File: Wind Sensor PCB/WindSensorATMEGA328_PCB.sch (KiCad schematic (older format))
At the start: 5 parts, among them P1 I2C, P2 SERIAL, P5 LOGO2, P6 PCB, P7 ENC

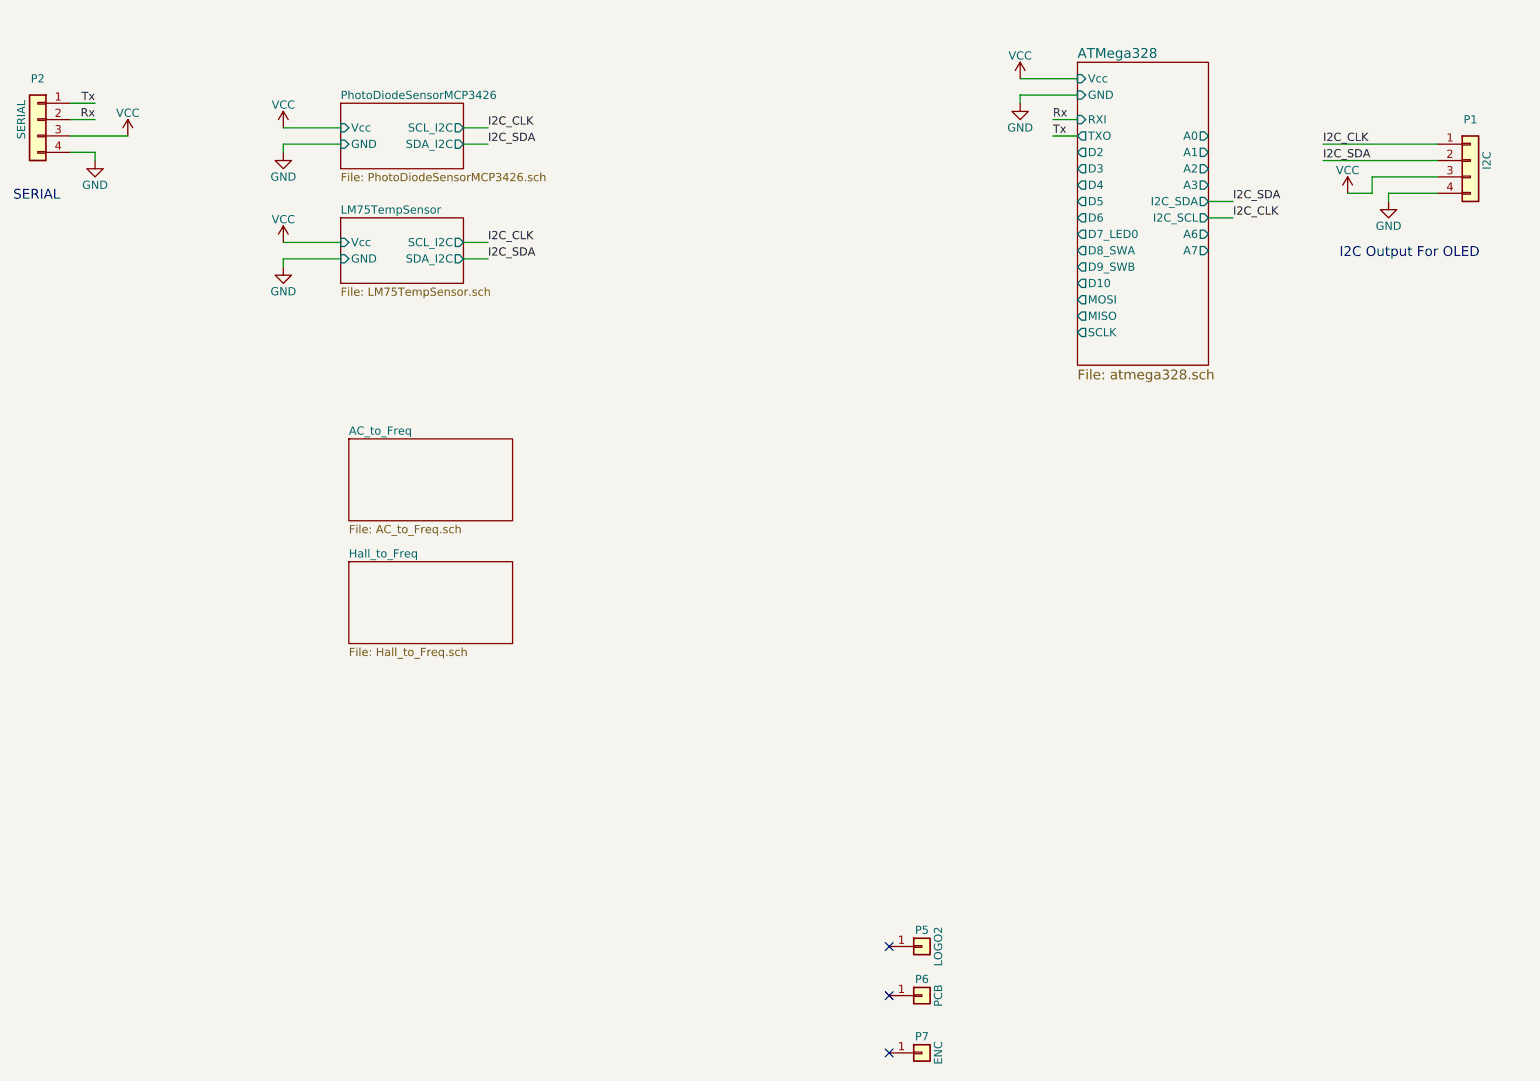
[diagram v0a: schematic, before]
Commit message: Updated PCB
Version 1 of the PCB with ATMEGA328 used...
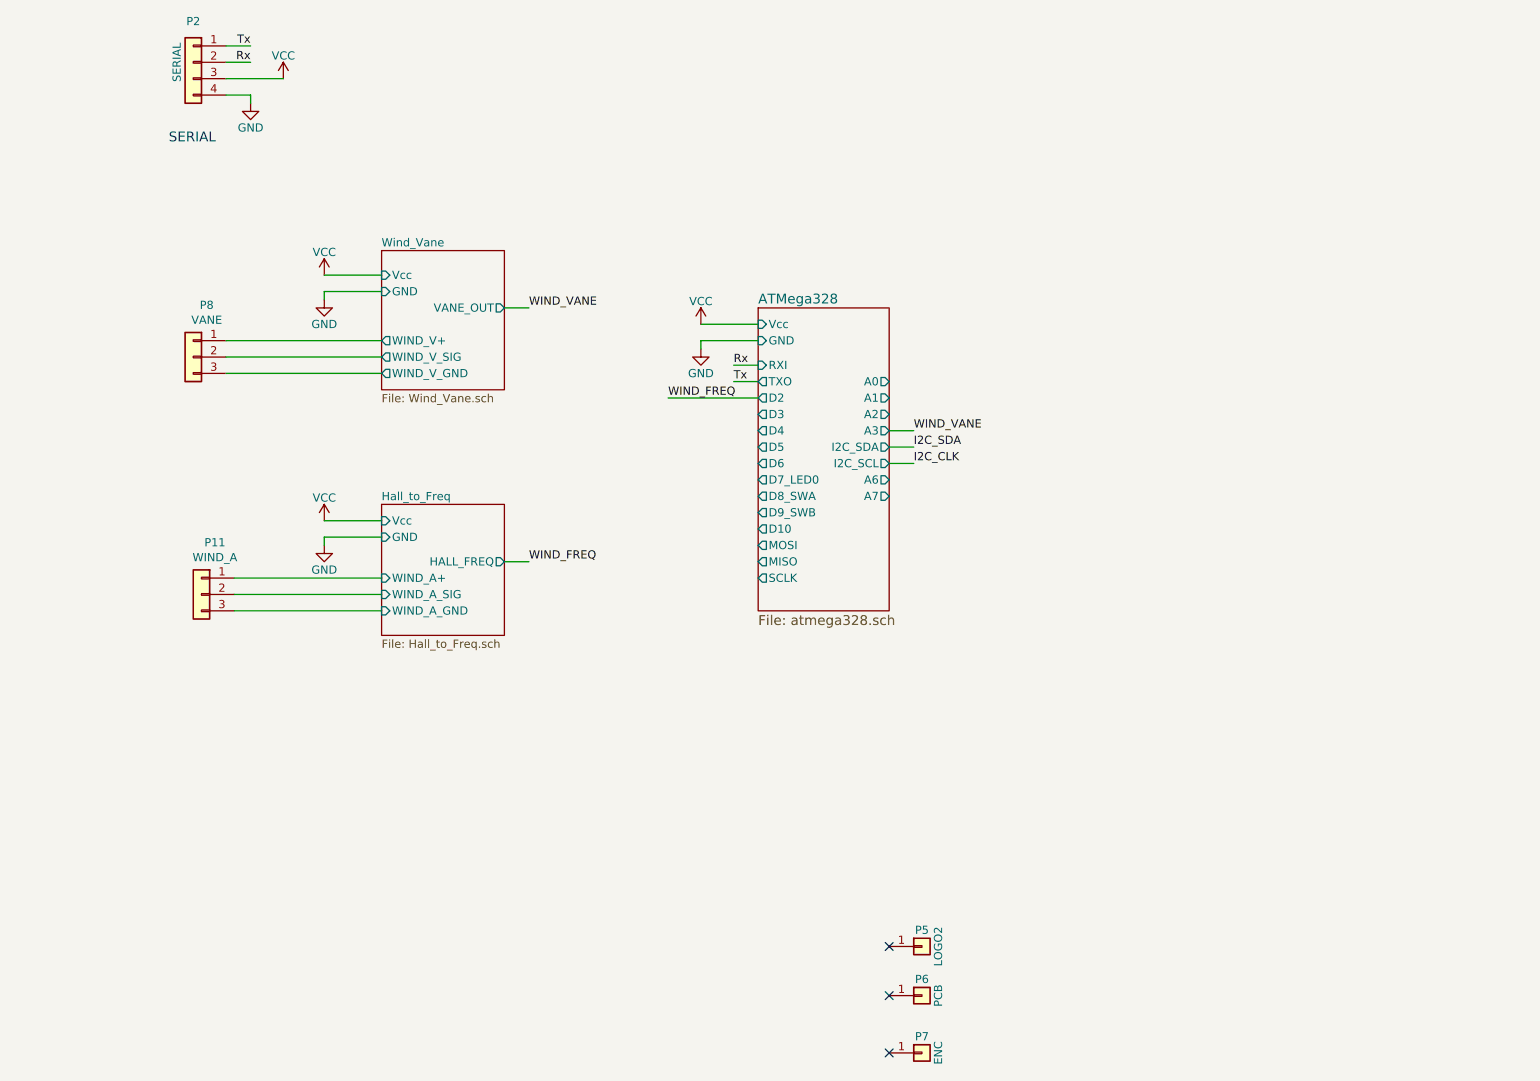
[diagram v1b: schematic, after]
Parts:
- removed P1: I2C, REInnovationFootprint:SIL-4_Grove_Not_Labelled, symbol Connector_Generic:Conn_01x04
- added P11: WIND_A, REInnovationFootprint:SIL-3_screw_terminal, symbol Connector_Generic:Conn_01x03
- added P8: VANE, REInnovationFootprint:SIL-3_screw_terminal, symbol Connector_Generic:Conn_01x03
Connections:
- new net Hall_to_Freq/WIND_A+: P11.1 (Pin_1)
- new net Hall_to_Freq/WIND_A_GND: P11.3 (Pin_3)
- new net Hall_to_Freq/WIND_A_SIG: P11.2 (Pin_2)
- new net Wind_Vane/WIND_V+: P8.1 (Pin_1)
- new net Wind_Vane/WIND_V_GND: P8.3 (Pin_3)
- new net Wind_Vane/WIND_V_SIG: P8.2 (Pin_2)
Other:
- note removed: "I2C Output For OLED"
- moved on the sheet: P2
